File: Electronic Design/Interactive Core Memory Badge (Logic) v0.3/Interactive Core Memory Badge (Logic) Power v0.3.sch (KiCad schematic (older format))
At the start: 16 parts, among them Q21 MMBT4401LT1G, SW1 SW_DPDT_x2

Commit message: Core logic board split to 5 sheets, power/driver sheet draft, pcb draft.
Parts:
- removed Q21: MMBT4401LT1G, Digikey:SOT-23-3, symbol Digikey-Transistors:MMBT4401LT1G
- removed R27: 470, Resistor_SMD:R_0805_2012Metric, symbol Device:R
- removed TP2: V-USB, TestPoint:TestPoint_Keystone_5000-5004_Miniature, symbol Connector:TestPoint
- removed TP6: VMEM, TestPoint:TestPoint_Keystone_5000-5004_Miniature, symbol Connector:TestPoint
- added C?: 1000uF, Capacitor_SMD:CP_Elec_8x10, symbol Device:CP1_Small
- added J3: Conn_01x03_Male, symbol Connector:Conn_01x03_Male
- added J4, J5: Conn_01x02_Male, symbol Connector:Conn_01x02_Male
- added TP7: 3V3_HP, TestPoint:TestPoint_Keystone_5000-5004_Miniature, symbol Connector:TestPoint
- added TP8: 3V3_LP, TestPoint:TestPoint_Keystone_5000-5004_Miniature, symbol Connector:TestPoint
- TP2: renamed from TP1; value V+USB -> 5V_VUSB
- TP5: renamed from TP7; value CCL -> SYS_CUR_LOW
- TP6: renamed from TP8; value CCH -> SYS_CUR_HI
- gave numbers to parts that had none: 2
- renumbered D13 to D1, TP4 to TP1, TP5 to TP4
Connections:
- net labels added: 3V3_100mA, 3V3_800mA, 5V_USB, FEATHER_3V3, FEATHER_GND, FEATHER_VBAT, FEATHER_VBUS, GND, TEENSY_3V3, TEENSY_GND, TEENSY_VIN, TEENSY_VUSB
- net labels removed: GNDPWR, V+USB, VMEM, WRITE_ENABLE
- wire segments 48 -> 51
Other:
- note added: "3.3V HIGH POWER SUPPLY"
- note added: "3.3V LOW POWER SUPPLY"
- note added: "BOTH MODES REQUIRE:\nVIN must be supplied TO the Teensy and\nthe Core 64 Logic Board provides it here."
- note added: "CORES AND ACCESSORIES"
- note added: "Diode provides 1.1V drop if using USB power.\n Keeps +VSW close to 4V to reduce 3.3V regulator strain.\n Prevents current flow back to USB and provides additional reverse polarity protection."
- note added: "HACKER POWER OPTION: ADAFRUIT FEATHER WITH REQUIRED LIPO\n*** MUST REMOVE ALKALINE/NIMH BATTERY PACK ***\nUSER MODIFICATION REQUIRED"
- note added: "HACKER UPGRADE TO USE FEATHER REQUIRES EITHER:\nA) REPLACE THE ALKALINE/NIMH BATTERY PACK WITH 1S LIPO IN THE SAME POWER PORT, OR ONE OF THE ALTERNATE PORTS\n>>> ALTERNATE CONNECTOR 1 - Adafruit (1769) SMT 2-pin JST-PH (used with the Feather and similar)\n>>> ALTERNATE CONNECTOR 2 - Generic SMT 2-pin .1” header option for everything else. \nB) REMOVE THE ALKALINE/NIMH BATTERY PACK AND CONNECT 1S 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"
- note added: "HIGH POWER SYSTEM GROUND"
- note added: "MODE 1\n BUILT-IN BATTERY PACK (Keystone 2482CN) WITH 4X “AAA” ALKALINE OR NIMH CELLS\n …or 3-4 “AA” alkaline/NiMh, or 1S LiPo, but the logic board does not recharge these batteries automatically from USB power.\n CONNECTED TO 3 PIN input for Battery Pack\n On PCB: SMT CONN, 3 TERM, HORZ, 2mm spacing, detent lock\n Such as: Keystone 976, JST PA BM03B-PASS-1-TFT(LF)(SN), Adafruit 4391 (JST PH 3-pi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"
- note added: "MODE 2\n USB 5V through Teensy LC or 3.2 \n VUSB is 5V from USB cable.\n VIN must be supplied TO the Teensy and Core 64 Logic Board provides it."
- note added: "MODE 3\n DIY 1S LIPO BATTERY 3-4V\n THE FEATHER WILL TRY TO CHARGE THIS WHEN USB POWER IS CONNECTED. \n FAILURE TO USE A 1S LIPO WILL DETROY THE CHARGER CIRCUIT."
- note added: "MODE 4\n USB 5V through the Feather.\n Automatically recharges a connected 1s LiPo."
- note added: "PLACE\nCAPACITOR\nNEAR\nLED MATRIX"
- note added: "POWER SWITCH"
- note added: "REVERSE POLARITY DETECTION AND SYSTEM\nCURRENT MEASUREMENT CLOSE TO BATTERY."
- note added: "REVERSE POLARITY PROTECTION"
- note added: "STAR GROUND AS MUCH AS POSSIBLE REVERSE\nPOLARITY FET TO GNDD (DIGITAL) AND GND (POWER)."
- note added: "SYSTEM CURRENT MEASUREMENT"
- note added: "TEENSY LC OR 3.2 AND ALKALINE/NIMH BATTERY PACK\n*** MUST CUT VIN-VUSB TRACE ***\nTHIS IS THE STANDARD MANUFACTURED KIT CONFIGURATION"
- note added: "TEENSY OR FEATHER 3.3V REGULATOR USED BY:\nAnalog reference, Core Sense Op-Amps, Magnetic Hall switches."
- note added: "TWO POWER MODES SELECTED BY DOUBLE-THROW SWITCH:"
- note removed: "1.1V DROP IF USING USB POWER\n(Keep +VSW close to 4V maximum.)"
- note removed: "All core power flows to ground through this resistor.\nCan this replace all of the others?\nAt least it can be used to measure current.\nCCL = Core Current Lowside Measurement\nCCH = Core Current Highside Measurement"
- note removed: "CORE POWER GROUND"
- note removed: "Core Memory Power"
- note removed: "IN: +BATT (3.7/4.2V) Battery is switched and fused\nOUT: +VSW\n"
- note removed: "IN: +VSW\nOUT: VMEM to cores controlled by WRITE_ENABLE"
- note removed: "IN: From computer USB 5V into Teensy LC module board (jumper cut on bottom of MCU onboard),\nOUT: V+USB and -BATT, and +3V3"
- note removed: "IN: V+USB (5V) into Micro LiPo Charger circuit to charge 1S battery\nOUT: as +BATT and to onboard connector 1S battery"
- note removed: "MCU, LED Array, I2C"
- note removed: "POWER FLOW:"
- note removed: "Power from USB or Battery\n* May not need to cut the jumper any more now???"
- note removed: "Reverse Polarity Protection FET"
- note removed: "STAR GROUND EVERYTHING TO -BATT"
- moved on the sheet: D1, F1, Q1, R1, SW1A, TP1, TP2, TP3, TP4, TP5, TP6, U1

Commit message: Add I2C bus, clean-up power symbols, update MCU sheet.
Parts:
- removed Q1: BS870, Package_TO_SOT_SMD:SOT-23, symbol Transistor_FET:BS870
- added Q?: IRLML6344TRPBF, Package_TO_SOT_SMD:SOT-23, symbol Transistor_FET:IRLML2060
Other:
- note added: "*** USE ONE 3V3 SOURCE AT A TIME ***"
- note added: "HACKER UPGRADE TO USE FEATHER REQUIRES EITHER:\nA) REPLACE THE ALKALINE/NIMH BATTERY PACK WITH 1S LIPO IN THE SAME POWER PORT, OR ONE OF THE ALTERNATE PORTS\n>>> ALTERNATE CONNECTOR 1 - Adafruit (1769) SMT 2-pin JST-PH (used with the Feather and Adafruit batteries)\n>>> ALTERNATE CONNECTOR 2 - Generic SMT 2-pin .1” header option for everything else. \nB) REMOVE THE ALKALINE/NIMH BATTERY PACK AND 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"
- note added: "LED ARRAY, TEENSY VIN"
- note added: "MODE 3\n USER REPLACED 1S LIPO BATTERY 3.7 OR 4.2V\n THE FEATHER WILL TRY TO CHARGE THE BATTERY AT 100MA WHEN USB POWER IS CONNECTED. \n FAILURE TO USE A 1S LIPO WILL DESTROY THE CHARGER CIRCUIT ON THE FEATHER."
- note added: "MODE 4\n USB 5V through the Feather.\n Automatically recharges a connected 1s LiPo at 100mA."
- note added: "REVERSE POLARITY DETECTION AND SYSTEM\nCURRENT MEASUREMENT CLOSE TO BATTERY.\n\nREF: https://www.instructables.com/id/Reverse-polarity-protection-for-your-circuit-with/\nIRLML6344TRPBF https://www.digikey.com/product-detail/en/infineon-technologies/IRLML6344TRPBF/IRLML6344TRPBFCT-ND/2538168"
- note added: "TEENSY OR FEATHER 3.3V REGULATOR USED BY:\nMCU, Analog reference, Core Sense Op-Amps, Magnetic Hall switches."
- note added: "TO DO: Does Feather receive power to MCU directly from battery?\nDoes Feather require a battery to be connected in order to work?"
- note added: "TO DO: Teensy and feather power to -Batt or GND? \nDo they need to avoid the reverse polarity detector? \nOr will they interfere?"
- note added: "TWO ALTERNATIVE POWER MODES SELECTED BY DOUBLE-THROW SWITCH:"
- note removed: "HACKER UPGRADE TO USE FEATHER REQUIRES EITHER:\nA) REPLACE THE ALKALINE/NIMH BATTERY PACK WITH 1S LIPO IN THE SAME POWER PORT, OR ONE OF THE ALTERNATE PORTS\n>>> ALTERNATE CONNECTOR 1 - Adafruit (1769) SMT 2-pin JST-PH (used with the Feather and similar)\n>>> ALTERNATE CONNECTOR 2 - Generic SMT 2-pin .1” header option for everything else. \nB) REMOVE THE ALKALINE/NIMH BATTERY PACK AND CONNECT 1S 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"
- note removed: "MODE 3\n DIY 1S LIPO BATTERY 3-4V\n THE FEATHER WILL TRY TO CHARGE THIS WHEN USB POWER IS CONNECTED. \n FAILURE TO USE A 1S LIPO WILL DETROY THE CHARGER CIRCUIT."
- note removed: "MODE 4\n USB 5V through the Feather.\n Automatically recharges a connected 1s LiPo."
- note removed: "REVERSE POLARITY DETECTION AND SYSTEM\nCURRENT MEASUREMENT CLOSE TO BATTERY."
- note removed: "TEENSY OR FEATHER 3.3V REGULATOR USED BY:\nAnalog reference, Core Sense Op-Amps, Magnetic Hall switches."
- moved on the sheet: TP7, U1
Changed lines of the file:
@@
 $EndComp
 Wire Wire Line
-	7050 5150 7250 5150
+	6950 5050 7150 5050
 Text GLabel 1000 5050 0    50   Input ~ 0
 5V_USB
@@
 	-1   0    0    1
 $EndComp
-Text Notes 700  7400 0    50   ~ 0
-REVERSE POLARITY DETECTION AND SYSTEM\nCURRENT MEASUREMENT CLOSE TO BATTERY.
+Text Notes 550  7750 0    50   ~ 0
+REVERSE POLARITY DETECTION AND SYSTEM\nCURRENT MEASUREMENT CLOSE TO BATTERY.\n\nREF: https://www.instructables.com/id/Reverse-polarity-protection-for-your-circuit-with/\nIRLML6344TRPBF https://www.digikey.com/product-detail/en/infineon-technologies/IRLML6344TRPBF/IRLML6344TRPBFCT-ND/2538168
 Wire Wire Line
 	850  6850 850  6950
 Wire Wire Line
 	5500 6950 5500 6850
-Text Notes 4650 7250 0    50   ~ 0
+Text Notes 4700 7250 0    50   ~ 0
 DIGITAL LOGIC GROUND
-Text Notes 6900 4650 0    50   ~ 0
+Text Notes 6800 4550 0    50   ~ 0
 CORES AND ACCESSORIES
 $Comp
@@
 $EndComp
 Wire Wire Line
-	7250 5150 7400 5150
-Connection ~ 7250 5150
-Wire Wire Line
-	7250 4900 7250 5150
+	7150 5050 7300 5050
+Connection ~ 7150 5050
+Wire Wire Line
+	7150 4800 7150 5050
 $Comp
 L Device:R R?
@@
 L Regulator_Linear:LD1117S33TR_SOT223 U1
 U 1 1 5E7B5B14
-P 6750 5150
+P 6650 5050
 AR Path="/5E7548ED/5E7B5B14" Ref="U1"  Part="1"
 AR Path="/5E755AC8/5D254AE8/5E7B5B14" Ref="U?"  Part="1"
-F 0 "U1" H 6750 5395 50  0000 C CNN
-F 1 "LD1117S33TR_SOT223" H 6750 5302 50  0000 C CNN
-F 2 "Package_TO_SOT_SMD:SOT-223-3_TabPin2" H 6750 5350 50  0001 C CNN
-F 3 "http://www.st.com/st-web-ui/static/active/en/resource/technical/document/datasheet/CD00000544.pdf" H 6850 4900 50  0001 C CNN
-	1    6750 5150
+F 0 "U1" H 6650 5295 50  0000 C CNN
+F 1 "LD1117S33TR_SOT223" H 6650 5202 50  0000 C CNN
+F 2 "Package_TO_SOT_SMD:SOT-223-3_TabPin2" H 6650 5250 50  0001 C CNN
+F 3 "http://www.st.com/st-web-ui/static/active/en/resource/technical/document/datasheet/CD00000544.pdf" H 6750 4800 50  0001 C CNN
+	1    6650 5050
 	1    0    0    -1
 $EndComp
 Text Notes 550  6200 0    118  ~ 0
 REVERSE POLARITY PROTECTION
-$Comp
-L Transistor_FET:BS870 Q1
-U 1 1 5E73C5E5
-P 1800 6750
-AR Path="/5E7548ED/5E73C5E5" Ref="Q1"  Part="1"
-AR Path="/5E755AC8/5D254AE8/5E73C5E5" Ref="Q?"  Part="1"
-F 0 "Q1" V 2051 6750 50  0000 C CNN
-F 1 "BS870" V 2144 6750 50  0000 C CNN
-F 2 "Package_TO_SOT_SMD:SOT-23" H 2000 6675 50  0001 L CIN
-F 3 "http://www.diodes.com/assets/Datasheets/ds11302.pdf" H 1800 6750 50  0001 L CNN
-	1    1800 6750
-	0    -1   1    0
-$EndComp
 Wire Wire Line
 	850  6850 1600 6850
 Wire Wire Line
-	6000 5150 6450 5150
+	6200 5050 6350 5050
 Text Notes 750  2200 0    50   ~ 0
 MODE 1\n  BUILT-IN BATTERY PACK (Keystone 2482CN) WITH 4X “AAA” ALKALINE OR NIMH CELLS\n  …or 3-4 “AA” alkaline/NiMh, or 1S LiPo, but the logic board does not recharge these batteries automatically from USB power.\n  CONNECTED TO 3 PIN input for Battery Pack\n  On PCB: SMT CONN, 3 TERM, HORZ, 2mm spacing, detent lock\n  Such as: Keystone 976, JST PA BM03B-PASS-1-TFT(LF)(SN), Adafruit 4391 (JST PH 3-pin aka STEMMA)\n  from KAWEEI Technology CW2001-03T-H01-BD-A,
@@
 TEENSY LC OR 3.2 AND ALKALINE/NIMH BATTERY PACK\n*** MUST CUT VIN-VUSB TRACE ***\nTHIS IS THE STANDARD MANUFACTURED KIT CONFIGURATION
 Text Notes 6150 1900 0    50   ~ 0
-HACKER UPGRADE TO USE FEATHER REQUIRES EITHER:\nA) REPLACE THE ALKALINE/NIMH BATTERY PACK WITH 1S LIPO IN THE SAME POWER PORT, OR ONE OF THE ALTERNATE PORTS\n>>> ALTERNATE CONNECTOR 1 - Adafruit (1769) SMT 2-pin JST-PH (used with the Feather and similar)\n>>> ALTERNATE CONNECTOR 2 - Generic SMT 2-pin .1” header option for everything else. \nB) REMOVE THE ALKALINE/NIMH BATTERY PACK AND CONNECT 1S LIPO DIRECTLY TO FEATHER JST-PH BATTERY/CHARGING PORT.
+HACKER UPGRADE TO USE FEATHER REQUIRES EITHER:\nA) REPLACE THE ALKALINE/NIMH BATTERY PACK WITH 1S LIPO IN THE SAME POWER PORT, OR ONE OF THE ALTERNATE PORTS\n>>> ALTERNATE CONNECTOR 1 - Adafruit (1769) SMT 2-pin JST-PH (used with the Feather and Adafruit batteries)\n>>> ALTERNATE CONNECTOR 2 - Generic SMT 2-pin .1” header option for everything else. \nB) REMOVE THE ALKALINE/NIMH BATTERY PACK AND CONNECT 1S LIPO DIRECTLY TO FEATHER JST-PH BATTERY/CHARGING PORT.
 Text Notes 6050 1200 0    100  ~ 0
 HACKER POWER OPTION: ADAFRUIT FEATHER WITH REQUIRED LIPO\n*** MUST REMOVE ALKALINE/NIMH BATTERY PACK ***\nUSER MODIFICATION REQUIRED
 Text Notes 6150 2100 0    50   ~ 0
-TWO POWER MODES SELECTED BY DOUBLE-THROW SWITCH:
+TWO ALTERNATIVE POWER MODES SELECTED BY DOUBLE-THROW SWITCH:
 Wire Wire Line
 	4500 3050 4800 3050
@@
 Text Notes 4000 2800 0    50   ~ 0
 BOTH MODES REQUIRE:\nVIN must be supplied TO the Teensy and\nthe Core 64 Logic Board provides it here.
-Text Notes 8550 4700 0    50   ~ 0
-TEENSY OR FEATHER 3.3V REGULATOR USED BY:\nAnalog reference, Core Sense Op-Amps, Magnetic Hall switches.
+Text Notes 8400 4650 0    50   ~ 0
+TEENSY OR FEATHER 3.3V REGULATOR USED BY:\nMCU, Analog reference, Core Sense Op-Amps, Magnetic Hall switches.
 Text GLabel 9100 5150 0    50   Input ~ 0
 FEATHER_3V3
@@
 Connection ~ 9350 5050
 Text Notes 6250 2500 0    50   ~ 0
-MODE 3\n  DIY 1S LIPO BATTERY 3-4V\n  THE FEATHER WILL TRY TO CHARGE THIS WHEN USB POWER IS CONNECTED. \n  FAILURE TO USE A 1S LIPO WILL DETROY THE CHARGER CIRCUIT.
+MODE 3\n  USER REPLACED 1S LIPO BATTERY 3.7 OR 4.2V\n  THE FEATHER WILL TRY TO CHARGE THE BATTERY AT 100MA WHEN USB POWER IS CONNECTED. \n  FAILURE TO USE A 1S LIPO WILL DESTROY THE CHARGER CIRCUIT ON THE FEATHER.
 $Comp
 L Connector:Conn_01x02_Male J5
@@
 	8350 2900 8900 2900
 Text Notes 6250 3350 0    50   ~ 0
-MODE 4\n  USB 5V through the Feather.\n  Automatically recharges a connected 1s LiPo.
+MODE 4\n  USB 5V through the Feather.\n  Automatically recharges a connected 1s LiPo at 100mA.
 Wire Wire Line
 	10050 2750 10400 2750
@@
 L power:+VSW #PWR0113
 U 1 1 5E8659D4
-P 6000 4950
+P 6200 4800
 AR Path="/5E7548ED/5E8659D4" Ref="#PWR0113"  Part="1"
 AR Path="/5E755AC8/5D254AE8/5E8659D4" Ref="#PWR?"  Part="1"
-F 0 "#PWR0113" H 6000 4800 50  0001 C CNN
-F 1 "+VSW" H 6015 5123 50  0000 C CNN
-F 2 "" H 6000 4950 50  0001 C CNN
-F 3 "" H 6000 4950 50  0001 C CNN
-	1    6000 4950
-	1    0    0    -1
-$EndComp
-Wire Wire Line
-	6000 4950 6000 5150
-Text GLabel 7400 5150 2    50   Input ~ 0
+F 0 "#PWR0113" H 6200 4650 50  0001 C CNN
+F 1 "+VSW" H 6215 4973 50  0000 C CNN
+F 2 "" H 6200 4800 50  0001 C CNN
+F 3 "" H 6200 4800 50  0001 C CNN
+	1    6200 4800
+	1    0    0    -1
+$EndComp
+Wire Wire Line
+	6200 4800 6200 5050
+Text GLabel 7300 5050 2    50   Input ~ 0
 3V3_800mA
 Wire Wire Line
@@
 L Connector:TestPoint TP7
 U 1 1 5E88DBA6
-P 7250 4900
+P 7150 4800
 AR Path="/5E7548ED/5E88DBA6" Ref="TP7"  Part="1"
 AR Path="/5E755AC8/5D254AE8/5E88DBA6" Ref="TP?"  Part="1"
-F 0 "TP7" H 7308 5018 50  0000 L CNN
-F 1 "3V3_HP" H 7308 4927 50  0000 L CNN
-F 2 "TestPoint:TestPoint_Keystone_5000-5004_Miniature" H 7450 4900 50  0001 C CNN
-F 3 "~" H 7450 4900 50  0001 C CNN
-	1    7250 4900
+F 0 "TP7" H 7208 4918 50  0000 L CNN
+F 1 "3V3_HP" H 7208 4827 50  0000 L CNN
+F 2 "TestPoint:TestPoint_Keystone_5000-5004_Miniature" H 7350 4800 50  0001 C CNN
+F 3 "~" H 7350 4800 50  0001 C CNN
+	1    7150 4800
 	1    0    0    -1
 $EndComp
@@
 L power:GND #PWR0115
 U 1 1 5E8C20D5
-P 6200 7150
+P 6200 6950
 AR Path="/5E7548ED/5E8C20D5" Ref="#PWR0115"  Part="1"
 AR Path="/5E755AC8/5D254AE8/5E8C20D5" Ref="#PWR?"  Part="1"
-F 0 "#PWR0115" H 6200 6900 50  0001 C CNN
-F 1 "GND" H 6205 6975 50  0000 C CNN
-F 2 "" H 6200 7150 50  0001 C CNN
-F 3 "" H 6200 7150 50  0001 C CNN
-	1    6200 7150
+F 0 "#PWR0115" H 6200 6700 50  0001 C CNN
+F 1 "GND" H 6205 6775 50  0000 C CNN
+F 2 "" H 6200 6950 50  0001 C CNN
+F 3 "" H 6200 6950 50  0001 C CNN
+	1    6200 6950
 	1    0    0    -1
 $EndComp
@@
 L power:GND #PWR0116
 U 1 1 5E8C4F56
-P 6750 5600
+P 6650 5500
 AR Path="/5E7548ED/5E8C4F56" Ref="#PWR0116"  Part="1"
 AR Path="/5E755AC8/5D254AE8/5E8C4F56" Ref="#PWR?"  Part="1"
-F 0 "#PWR0116" H 6750 5350 50  0001 C CNN
-F 1 "GND" H 6755 5425 50  0000 C CNN
-F 2 "" H 6750 5600 50  0001 C CNN
-F 3 "" H 6750 5600 50  0001 C CNN
-	1    6750 5600
-	1    0    0    -1
-$EndComp
-Wire Wire Line
-	6750 5450 6750 5600
+F 0 "#PWR0116" H 6650 5250 50  0001 C CNN
+F 1 "GND" H 6655 5325 50  0000 C CNN
+F 2 "" H 6650 5500 50  0001 C CNN
+F 3 "" H 6650 5500 50  0001 C CNN
+	1    6650 5500
+	1    0    0    -1
+$EndComp
+Wire Wire Line
+	6650 5350 6650 5500
 Connection ~ 5500 6850
 Wire Wire Line
@@
 SYSTEM CURRENT MEASUREMENT
 Wire Wire Line
-	6200 7150 6200 6850
+	6200 6950 6200 6850
 Wire Wire Line
 	6200 6850 5500 6850
-Text Notes 5600 7500 0    50   ~ 0
+Text Notes 5750 7250 0    50   ~ 0
 HIGH POWER SYSTEM GROUND
 Wire Wire Line
@@
 	1    0    0    -1
 $EndComp
-Text Notes 6750 5900 0    50   ~ 0
+Text Notes 6650 5800 0    50   ~ 0
 HIGH POWER SYSTEM GROUND
 Text Notes 4400 5550 0    50   ~ 0
@@
 Text Notes 2050 3850 0    50   ~ 0
 HIGH POWER SYSTEM GROUND
-Text Notes 3050 7600 0    50   ~ 0
+Text Notes 4900 7450 0    50   ~ 0
 STAR GROUND AS MUCH AS POSSIBLE REVERSE\nPOLARITY FET TO GNDD (DIGITAL) AND GND (POWER).
+Text Notes 8550 5300 0    50   ~ 0
+*** USE ONE 3V3 SOURCE AT A TIME ***
+Text Notes 3800 4400 0    50   ~ 0
+LED ARRAY, TEENSY VIN
+Text Notes 8550 3600 0    50   ~ 10
+TO DO: Does Feather receive power to MCU directly from battery?\nDoes Feather require a battery to be connected in order to work?
+$Comp
+L Transistor_FET:IRLML2060 Q?
+U 1 1 5E770BB5
+P 1800 6750
+F 0 "Q?" V 2051 6750 50  0000 C CNN
+F 1 "IRLML6344TRPBF" V 2144 6750 50  0000 C CNN
+F 2 "Package_TO_SOT_SMD:SOT-23" H 2000 6675 50  0001 L CIN
+F 3 "https://www.digikey.com/product-detail/en/infineon-technologies/IRLML6344TRPBF/IRLML6344TRPBFCT-ND/2538168" H 1800 6750 50  0001 L CNN
+	1    1800 6750
+	0    1    1    0
+$EndComp
+Text Notes 3200 3650 0    50   ~ 10
+TO DO: Teensy and feather power to -Batt or GND? \nDo they need to avoid the reverse polarity detector? \nOr will they interfere?
 $EndSCHEMATC

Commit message: Add sense NORs and IO expansion and NOTs.
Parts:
- gave numbers to parts that had none: 2
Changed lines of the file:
@@
 $Descr A4 11693 8268
 encoding utf-8
-Sheet 2 5
+Sheet 2 6
 Title "Core 64 - Power Schematic"
 Date "2020-03-15"
@@
 AR Path="/5E755AC8/5D2551FF/5E90E57B" Ref="C?"  Part="1"
 AR Path="/5E755AC8/5E90E57B" Ref="C?"  Part="1"
-AR Path="/5E7548ED/5E90E57B" Ref="C?"  Part="1"
-F 0 "C?" H 4550 5200 50  0000 L CNN
+AR Path="/5E7548ED/5E90E57B" Ref="C3"  Part="1"
+F 0 "C3" H 4550 5200 50  0000 L CNN
 F 1 "1000uF" H 4550 5100 50  0000 L CNN
 F 2 "Capacitor_SMD:CP_Elec_8x10" H 4450 5100 50  0001 C CNN
@@
 	4450 4950 4450 5000
 $Comp
-L power:GND #PWR?
+L power:GND #PWR0119
 U 1 1 5E9A5B3C
 P 4450 5250
-AR Path="/5E7548ED/5E9A5B3C" Ref="#PWR?"  Part="1"
+AR Path="/5E7548ED/5E9A5B3C" Ref="#PWR0119"  Part="1"
 AR Path="/5E755AC8/5D254AE8/5E9A5B3C" Ref="#PWR?"  Part="1"
-F 0 "#PWR?" H 4450 5000 50  0001 C CNN
+F 0 "#PWR0119" H 4450 5000 50  0001 C CNN
 F 1 "GND" H 4455 5075 50  0000 C CNN
 F 2 "" H 4450 5250 50  0001 C CNN
@@
 TO DO: Does Feather receive power to MCU directly from battery?\nDoes Feather require a battery to be connected in order to work?
 $Comp
-L Transistor_FET:IRLML2060 Q?
+L Transistor_FET:IRLML2060 Q1
 U 1 1 5E770BB5
 P 1800 6750
-F 0 "Q?" V 2051 6750 50  0000 C CNN
+F 0 "Q1" V 2051 6750 50  0000 C CNN
 F 1 "IRLML6344TRPBF" V 2144 6750 50  0000 C CNN
 F 2 "Package_TO_SOT_SMD:SOT-23" H 2000 6675 50  0001 L CIN

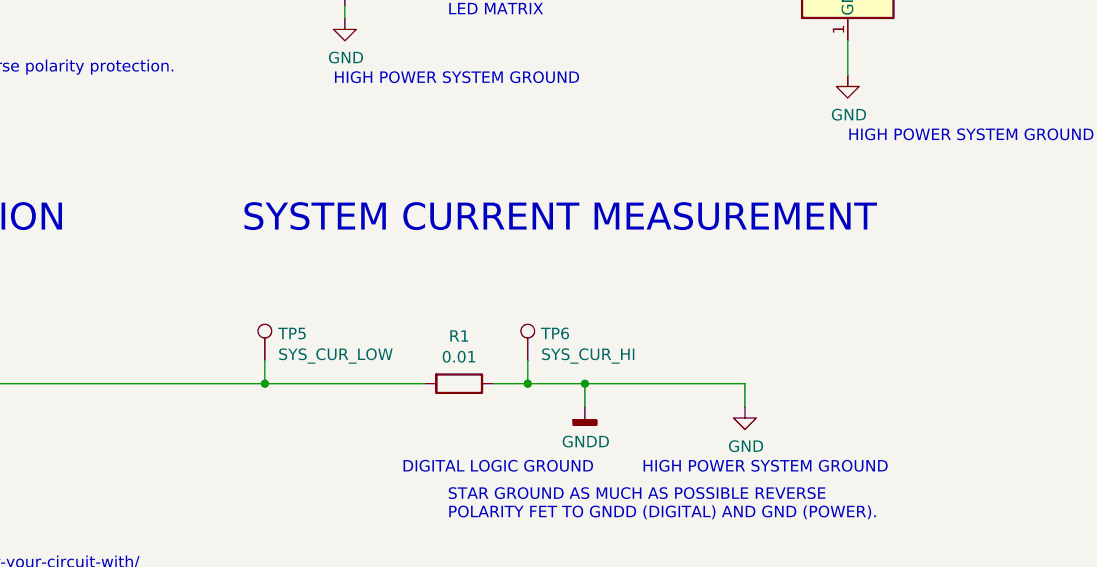
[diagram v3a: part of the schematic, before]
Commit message: Create PDF schematics
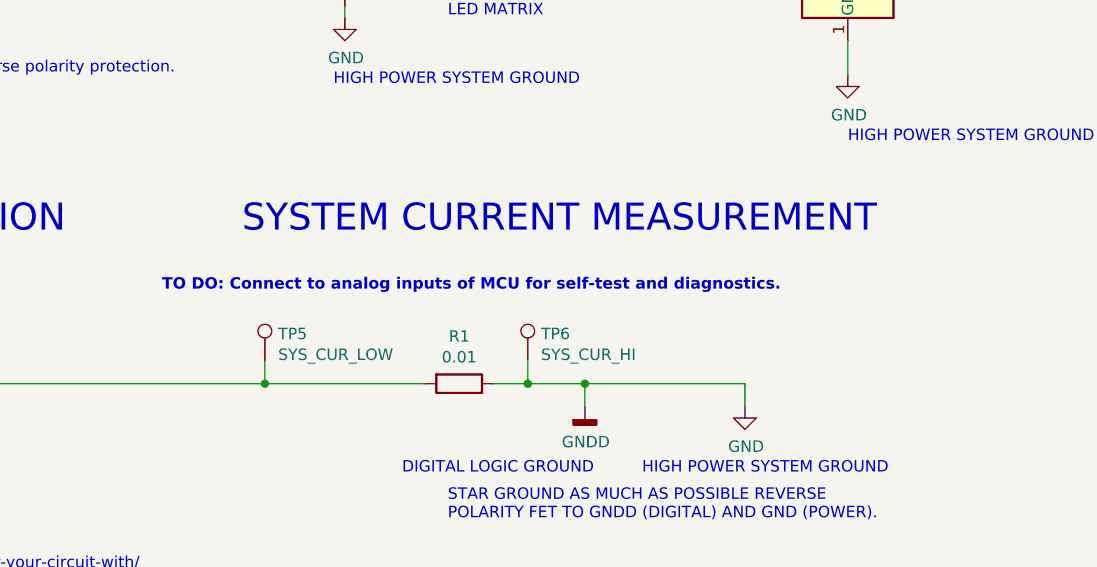
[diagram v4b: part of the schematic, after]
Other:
- note added: "TO DO: Connect to analog inputs of MCU for self-test and diagnostics."
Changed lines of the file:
@@
 Text Notes 3200 3650 0    50   ~ 10
 TO DO: Teensy and feather power to -Batt or GND? \nDo they need to avoid the reverse polarity detector? \nOr will they interfere?
+Text Notes 3650 6450 0    50   ~ 10
+TO DO: Connect to analog inputs of MCU for self-test and diagnostics.
 $EndSCHEMATC
